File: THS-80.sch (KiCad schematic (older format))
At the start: 36 parts, among them J1 RC80 Bus, J4 IDE, J8 USB_B_Micro, SW1 Reset, U1 DS1813R-5+T&R, U12 MAX40200AUK, U3 CPU -Z84C0020AEG, U6 SRAM - IS62C5128BL-45TLI, U8 SST39SF040

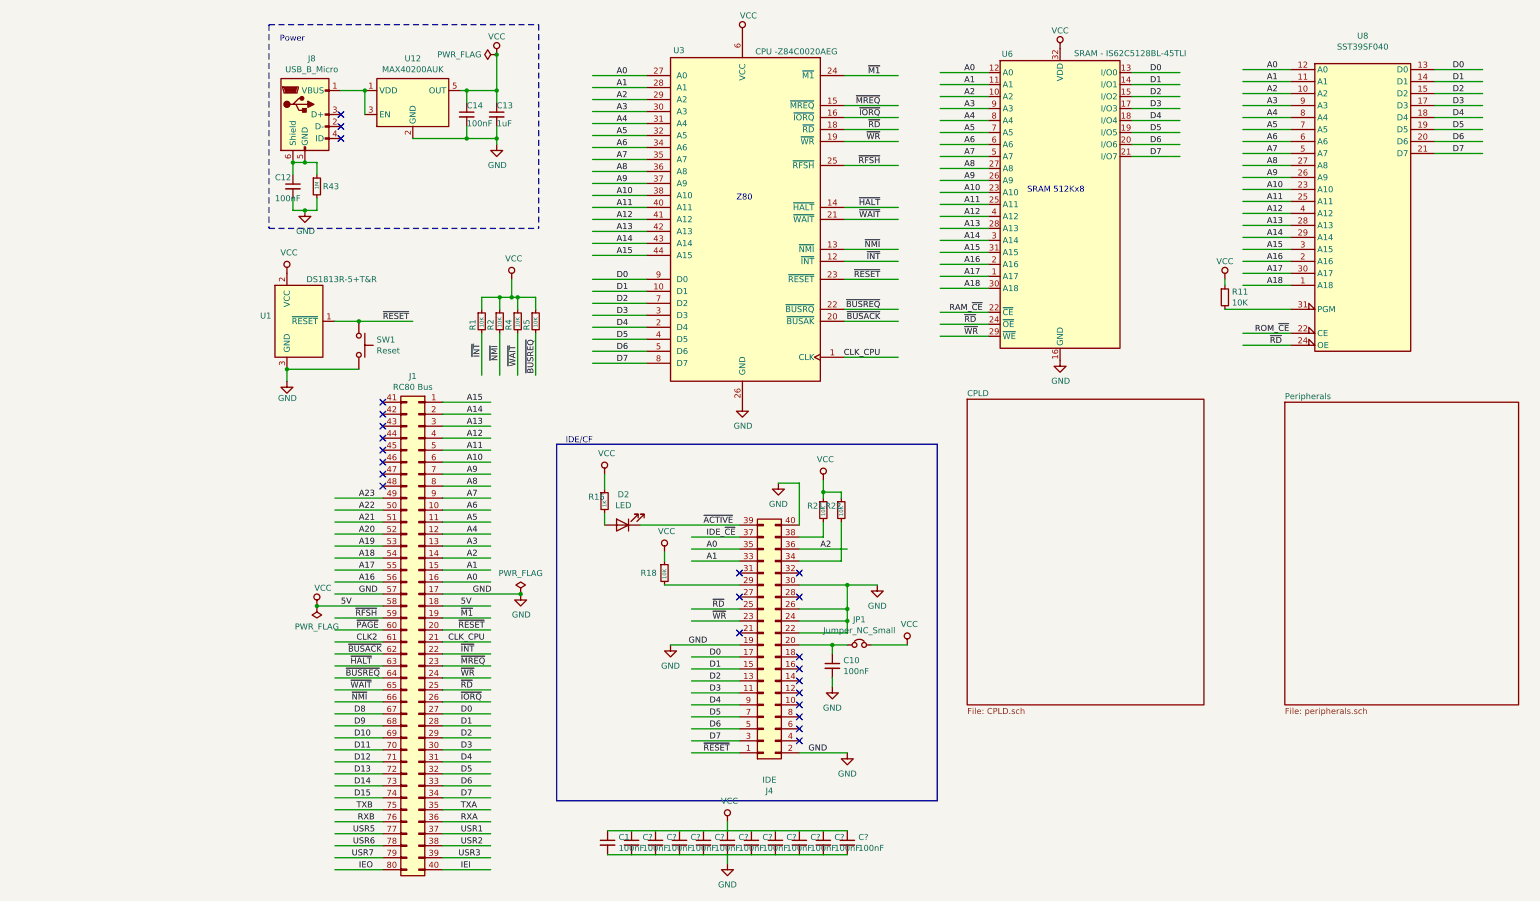
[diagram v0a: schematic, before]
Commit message: reset annotations, added dip switch
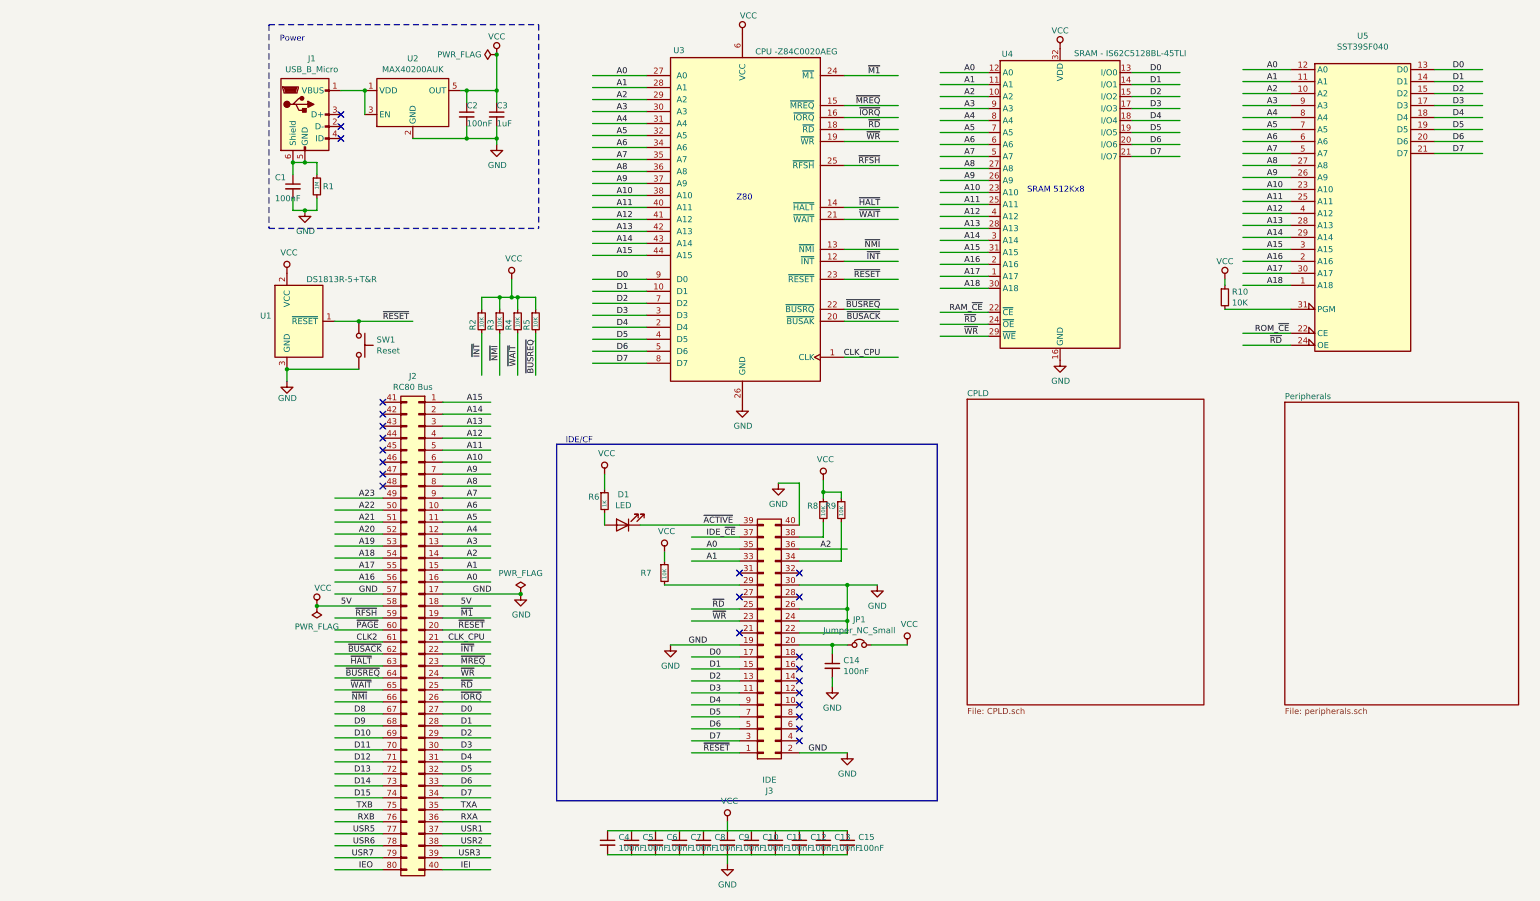
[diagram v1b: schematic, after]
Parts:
- gave numbers to parts that had none: 10
- renumbered C12 to C1, C10 to C14, C14 to C2, C13 to C3, C1 to C4, D2 to D1, J8 to J1, J1 to J2, J4 to J3, R43 to R1, R11 to R10, R1 to R2, R2 to R3, R16 to R6, R18 to R7, R21 to R8, R22 to R9, U12 to U2, U6 to U4, U8 to U5

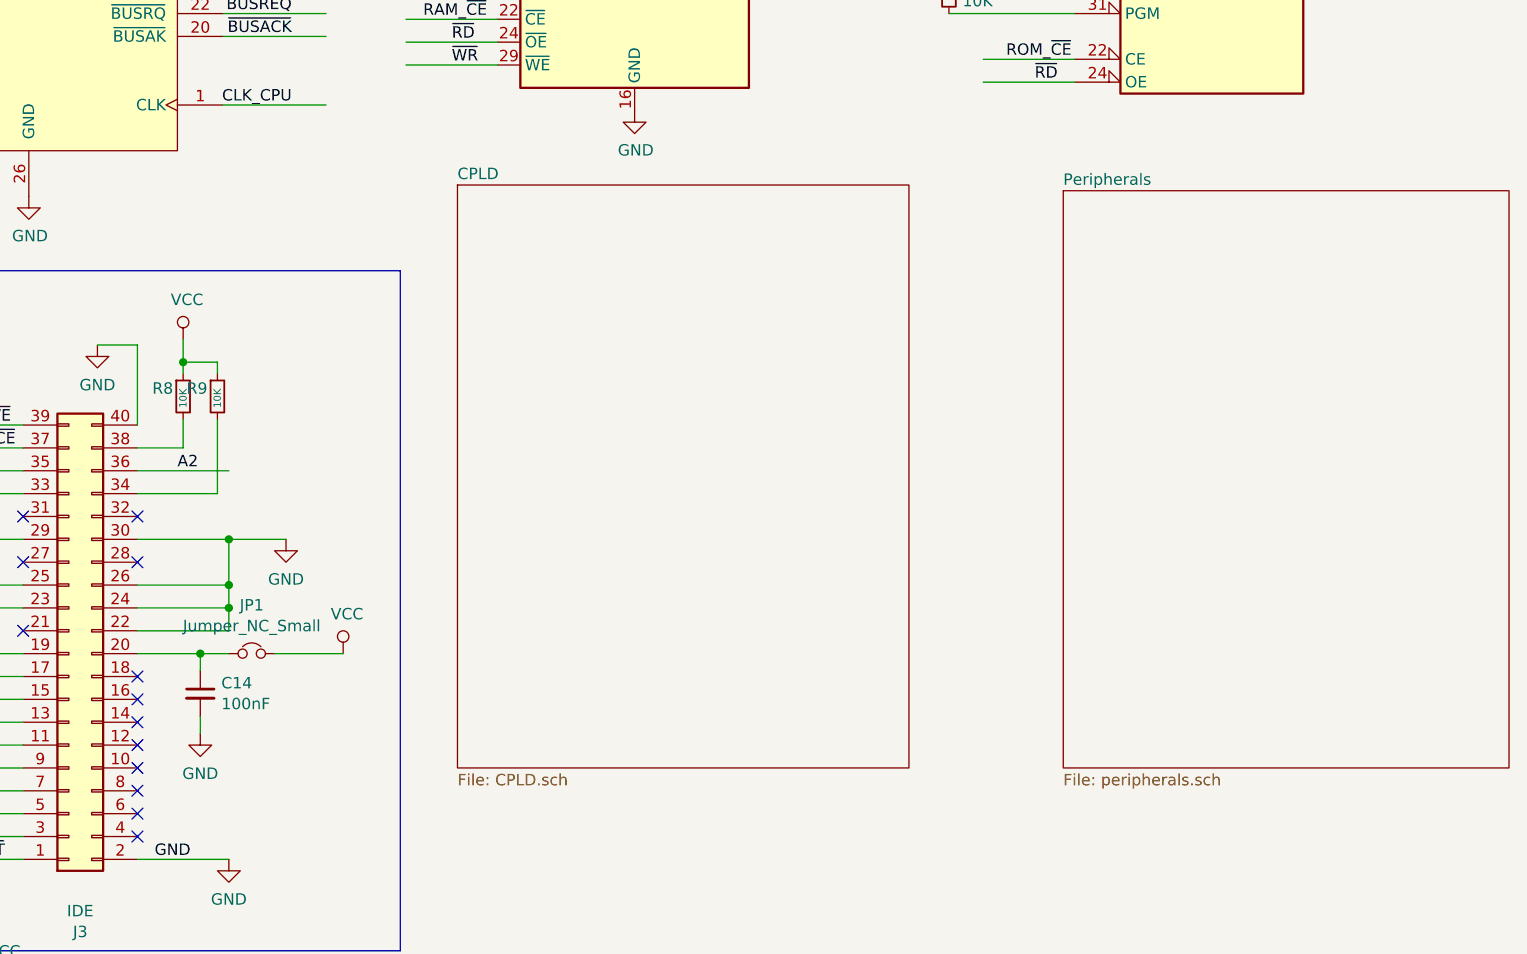
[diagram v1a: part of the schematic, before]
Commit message: connect sheet pins
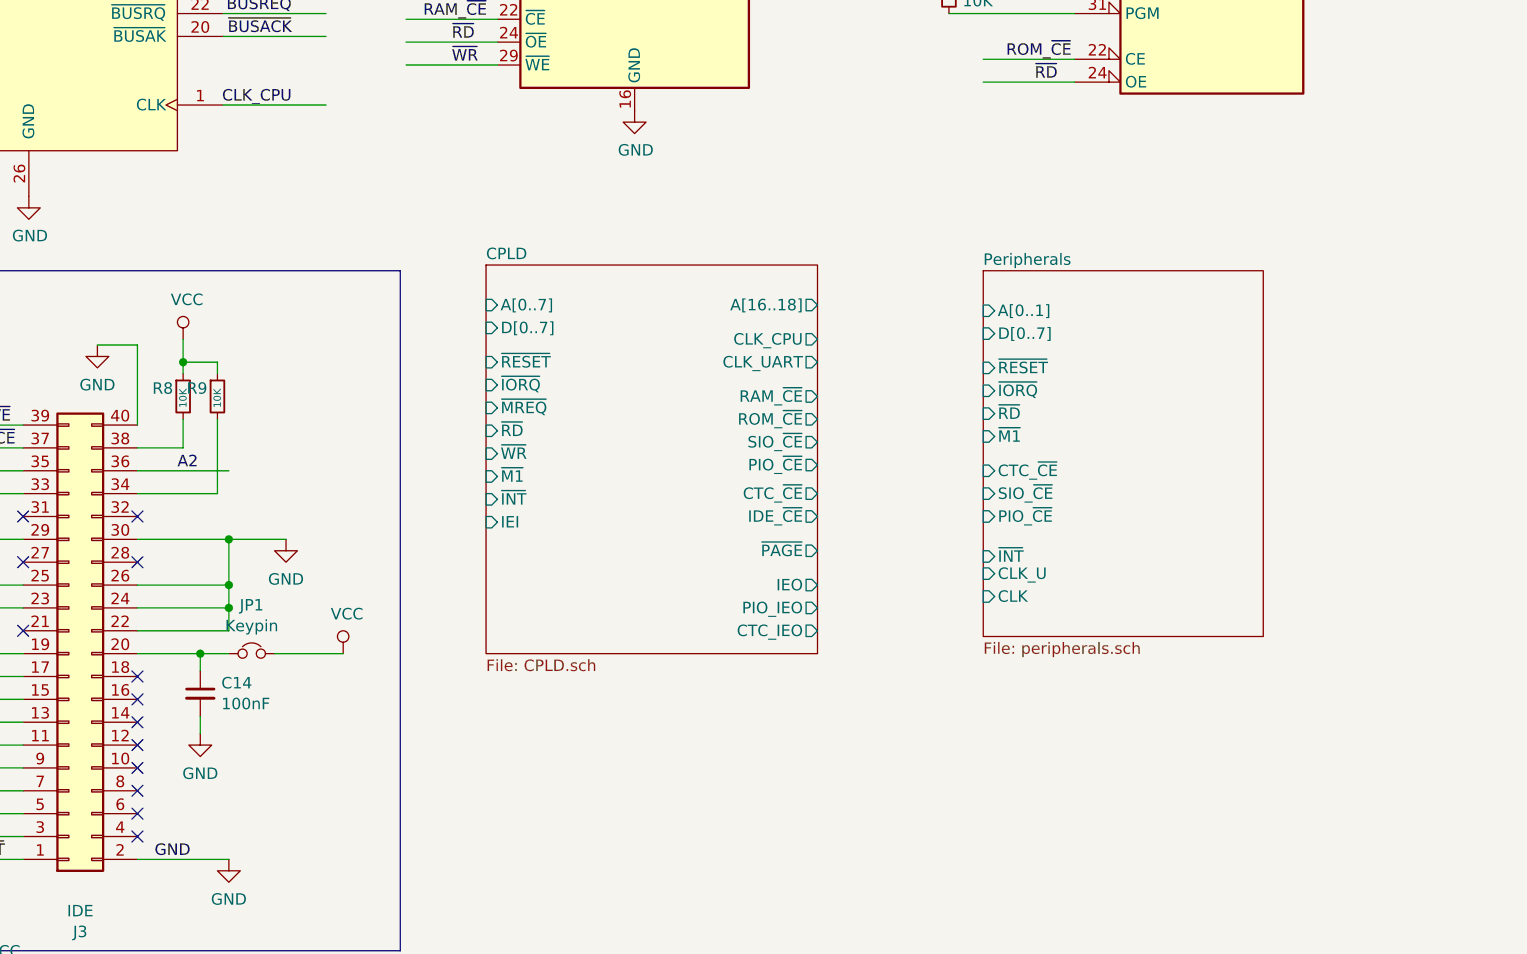
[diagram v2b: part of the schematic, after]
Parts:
- JP1: value Jumper_NC_Small -> Keypin
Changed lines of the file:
@@
 P 5525 5800
 F 0 "JP1" H 5525 6012 50  0000 C CNN
-F 1 "Jumper_NC_Small" H 5525 5921 50  0000 C CNN
+F 1 "Keypin" H 5525 5921 50  0000 C CNN
 F 2 "Connector_PinHeader_2.54mm:PinHeader_1x02_P2.54mm_Vertical" H 5525 5800 50  0001 C CNN
 F 3 "~" H 5525 5800 50  0001 C CNN
@@
 Wire Wire Line
 	5300 6075 5300 6150
-$Sheet
-S 6425 3750 1975 2550
-U 5D70CA34
-F0 "CPLD" 50
-F1 "CPLD.sch" 50
-$EndSheet
 Wire Notes Line
 	2850 625  2850 2325
@@
 	600  625  600  2325
 $Sheet
-S 9075 3775 1950 2525
+S 8725 4125 1225 1600
 U 5DFE5C15
 F0 "Peripherals" 50
 F1 "peripherals.sch" 50
+F2 "D[0..7]" I L 8725 4400 50
+F3 "A[0..1]" I L 8725 4300 50
+F4 "~RESET" I L 8725 4550 50
+F5 "CLK" I L 8725 5550 50
+F6 "CTC_~CE" I L 8725 5000 50
+F7 "~M1" I L 8725 4850 50
+F8 "~IORQ" I L 8725 4650 50
+F9 "~RD" I L 8725 4750 50
+F10 "SIO_~CE" I L 8725 5100 50
+F11 "PIO_~CE" I L 8725 5200 50
+F12 "~INT" I L 8725 5375 50
+F13 "CLK_U" I L 8725 5450 50
 $EndSheet
 Wire Wire Line
@@
 Wire Wire Line
 	3425 7350 3625 7350
+$Sheet
+S 6550 4100 1450 1700
+U 5D70CA34
+F0 "CPLD" 50
+F1 "CPLD.sch" 50
+F2 "A[0..7]" I L 6550 4275 50
+F3 "A[16..18]" O R 8000 4275 50
+F4 "D[0..7]" I L 6550 4375 50
+F5 "~RESET" I L 6550 4525 50
+F6 "~IORQ" I L 6550 4625 50
+F7 "~MREQ" I L 6550 4725 50
+F8 "~RD" I L 6550 4825 50
+F9 "~WR" I L 6550 4925 50
+F10 "~M1" I L 6550 5025 50
+F11 "RAM_~CE" O R 8000 4675 50
+F12 "ROM_~CE" O R 8000 4775 50
+F13 "SIO_~CE" O R 8000 4875 50
+F14 "PIO_~CE" O R 8000 4975 50
+F15 "CTC_~CE" O R 8000 5100 50
+F16 "IDE_~CE" O R 8000 5200 50
+F17 "~PAGE" O R 8000 5350 50
+F18 "CLK_CPU" O R 8000 4425 50
+F19 "CLK_UART" O R 8000 4525 50
+F20 "CTC_IEO" O R 8000 5700 50
+F21 "~INT" I L 6550 5125 50
+F22 "IEI" I L 6550 5225 50
+F23 "IEO" O R 8000 5500 50
+F24 "PIO_IEO" O R 8000 5600 50
+$EndSheet
 $EndSCHEMATC

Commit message: connected sheet pins to bus
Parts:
- added J10: RC80 Bus, Connector_PinSocket_2.54mm:PinSocket_2x40_P2.54mm_Vertical, symbol Connector_Generic:Conn_02x40_Odd_Even
- J2: footprint Connector_PinHeader_2.54mm:PinHeader_2x40_Top_Bottom_P2.54mm_Horizontal -> Connector_PinSocket_2.54mm:PinSocket_2x40_P2.54mm_Horizontal; symbol Connector_Generic:Conn_02x40_Top_Bottom -> Connector_Generic:Conn_02x40_Odd_Even
- J3: footprint Connector_PinHeader_2.54mm:PinHeader_2x20_P2.54mm_Horizontal -> Connector_Multicomp:Multicomp_MC9A12-4034_2x20_P2.54mm_Vertical
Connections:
- net labels added: A[0..1], A[0..7], A[16..18], CLK_U, CTC_~CE, D[0..7], PIO_~CE, SIO_~CE
- wire segments 275 -> 381
- no-connect marks 24 -> 32
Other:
- note added: "Flash/ROM"

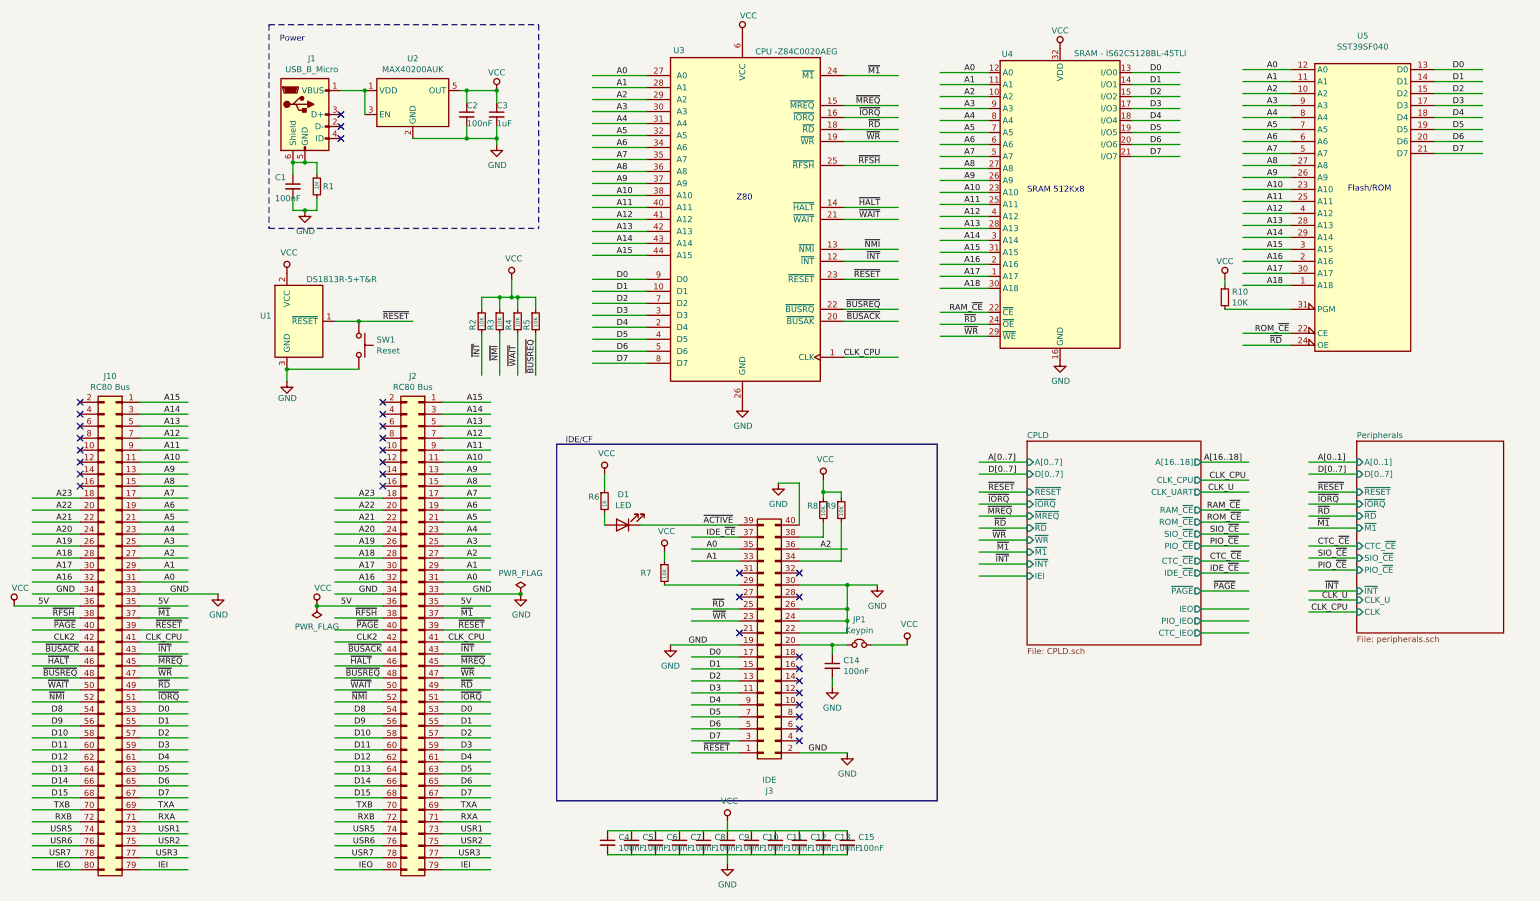
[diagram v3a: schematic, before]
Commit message: Moved CPU, RAM, ROM to sub-sheet
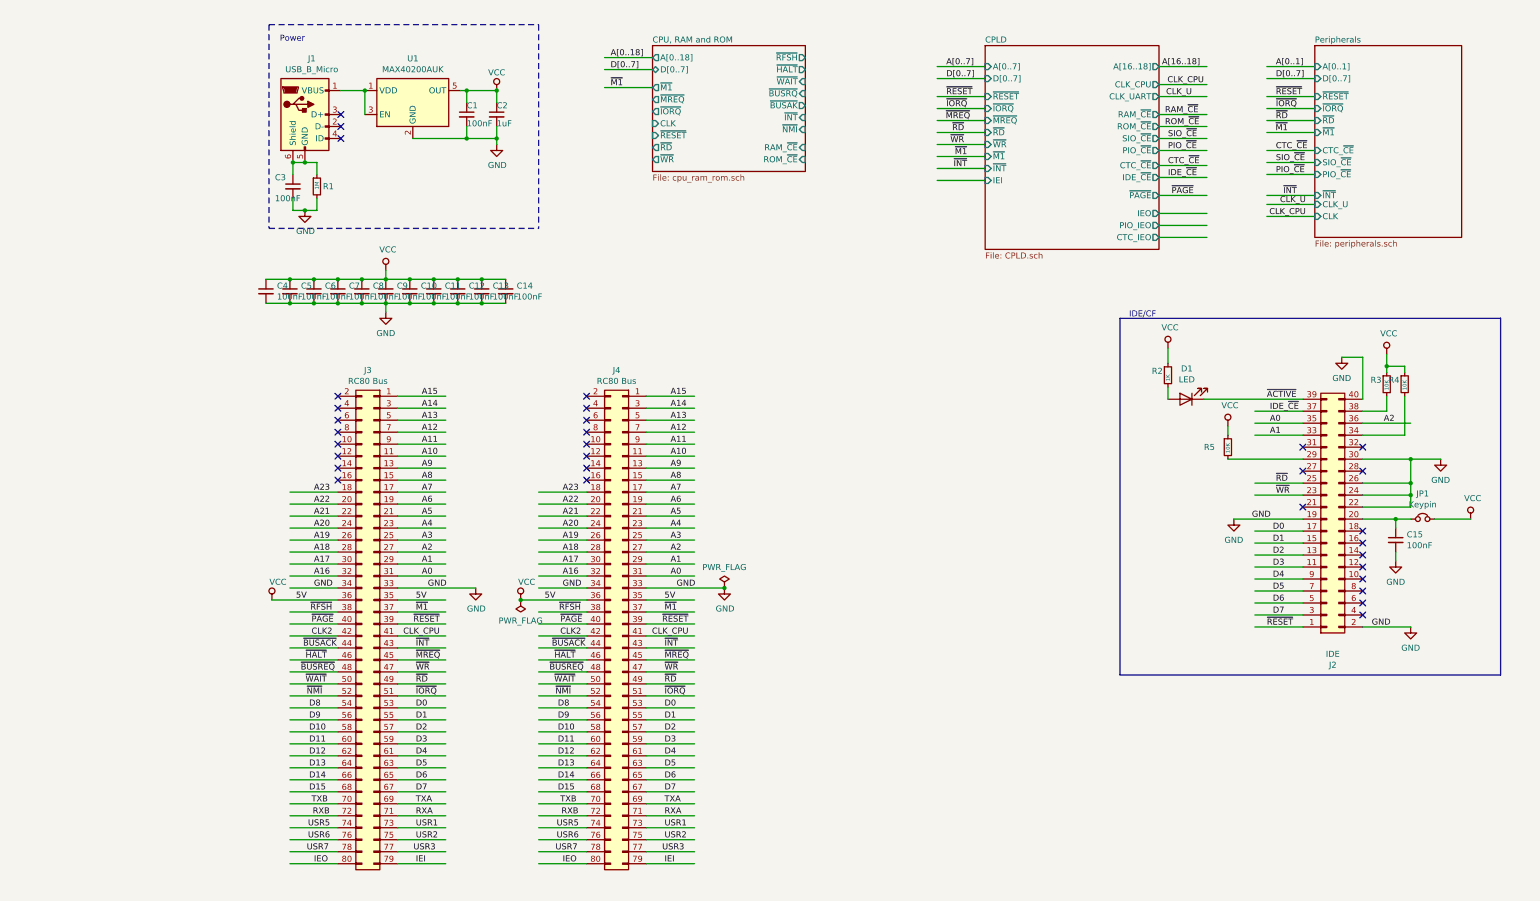
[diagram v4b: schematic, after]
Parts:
- removed R10, R2, R3, R4, R5: 10K, Resistor_SMD:R_0603_1608Metric_Pad1.05x0.95mm_HandSolder, symbol Device:R_Small
- removed SW1: Reset, Button_Switch_SMD:SW_Push_SPST_NO_Alps_SKRK, symbol Switch:SW_Push
- removed U1: DS1813R-5+T&R, Package_TO_SOT_SMD:SOT-23, symbol THS-80:DS1813R-5+T&R
- removed U3: CPU -Z84C0020AEG, Package_QFP:LQFP-44_10x10mm_P0.8mm, symbol THS-80:Z84C0010AEG
- removed U4: SRAM - IS62C5128BL-45TLI, Package_SO:TSOP-II-32_21.0x10.2mm_P1.27mm, symbol THS-80:IS62C5128BL-45TLI
- removed U5: SST39SF040, Package_LCC:PLCC-32_SMD-Socket, symbol Memory_Flash:SST39SF040
- renumbered C2 to C1, C15 to C14, C14 to C15, C3 to C2, C1 to C3, J3 to J2, J10 to J3, J2 to J4, R6 to R2, R8 to R3, R9 to R4, R7 to R5, U2 to U1
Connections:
- net labels added: A[0..18]
- wire segments 381 -> 268
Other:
- note removed: "Flash/ROM"
- note removed: "SRAM 512Kx8"
- note removed: "Z80"
- moved on the sheet: C10, C11, C12, C13, C14, C15, C4, C5, C6, C7, C8, C9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
